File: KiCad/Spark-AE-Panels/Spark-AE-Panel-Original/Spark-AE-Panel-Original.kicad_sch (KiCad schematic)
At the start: 8 parts, among them U7 Connector_Micro_SD_Card_Yamai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

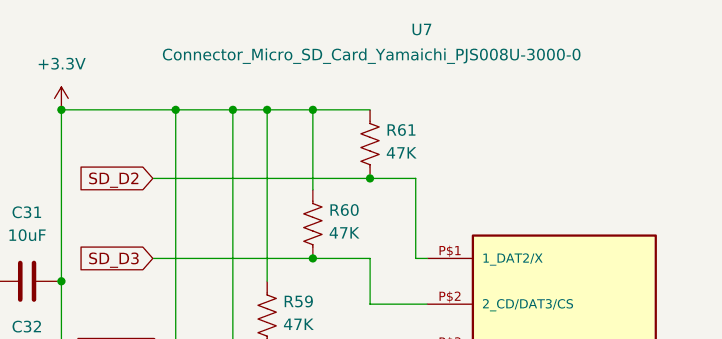
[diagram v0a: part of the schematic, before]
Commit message: rough pass over original mk0.1 panel. needs confirmation.
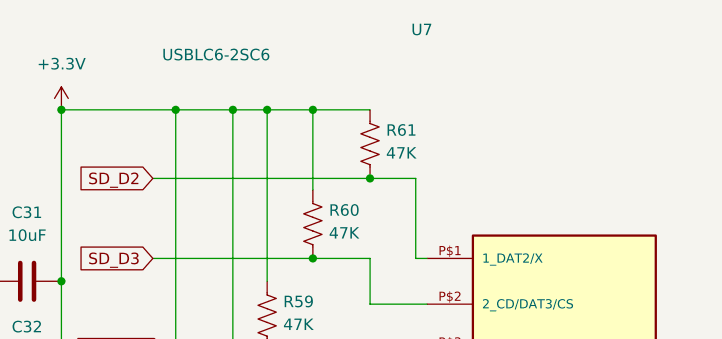
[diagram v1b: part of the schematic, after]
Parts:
- U7: value Connector_Micro_SD_Card_Yamaichi_PJS008U-3000-0 -> USBLC6-2SC6; footprint clectric-diy:PJS008U-3000-0 -> Package_TO_SOT_SMD:SOT-23-6; Availability In Stock -> (none); Check_prices https://www.snapeda.com/parts/PJS008U-3000-0/Yamaichi/view-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 -> (none); Description_1 8 Position Card Connector Secure Digital - microSD™ Through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 -> (none); MF Yamaichi -> (none); MP PJS008U-3000-0 -> (none); Package None -> (none); Price None -> (none); Purchase-URL https://www.snapeda.com/api/url_track_click_mouser/?unipart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 -> (none); SnapEDA_Link https://www.snapeda.com/parts/PJS008U-3000-0/Yamaichi/view-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 -> (none)
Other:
- title: Spark-AE -> Spark-AE-Panel-Original
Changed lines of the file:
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@@
 	(paper "A4")
 	(title_block
-		(title "Spark-AE")
-		(date "2026-01-14")
+		(title "Spark-AE-Panel-Original")
+		(date "2026-04-26")
+		(rev "Mk0.1")
 		(company "Copyright © 2026 clectric.diy Licensed under CERN-OHL-S v2")
 		(comment 1 "Charles H. Leggett")
@@
 		)
 		(instances
-			(project "Spark-AE-Panel"
+			(project "Spark-AE-Panel-Original"
 				(path "/3edf45fb-9cc6-4079-8dcc-c280276ec612"
 					(reference "R59")
@@
 		)
 		(instances
-			(project "Spark-AE-Panel"
+			(project "Spark-AE-Panel-Original"
 				(path "/3edf45fb-9cc6-4079-8dcc-c280276ec612"
 					(reference "#PWR066")
@@
 		)
 		(instances
-			(project "Spark-AE-Panel"
+			(project "Spark-AE-Panel-Original"
 				(path "/3edf45fb-9cc6-4079-8dcc-c280276ec612"
 					(reference "#PWR063")
@@
 			)
 		)
-		(property "Value" "Connector_Micro_SD_Card_Yamaichi_PJS008U-3000-0"
+		(property "Value" "USBLC6-2SC6"
 			(at 102.616 53.594 90)
 			(show_name no)
@@
 			)
 		)
-		(property "Footprint" "clectric-diy:PJS008U-3000-0"
+		(property "Footprint" "Package_TO_SOT_SMD:SOT-23-6"
 			(at 147.32 99.06 0)
 			(hide yes)
@@
 			)
 		)
-		(property "Datasheet" ""
+		(property "Datasheet" "https://www.st.com/resource/en/datasheet/usblc6-2.pdf"
 			(at 147.32 99.06 0)
 			(hide yes)
@@
 			)
 		)
-		(property "Description" ""
+		(property "Description" "Very low capacitance ESD protection diode, 2 data-line, SOT-23-6"
 			(at 147.32 99.06 0)
 			(hide yes)
@@
 			)
 		)
-		(property "MF" "Yamaichi"
-			(at 147.32 99.06 0)
-			(hide yes)
-			(show_name no)
-			(do_not_autoplace no)
-			(effects
-				(font
-					(size 1.27 1.27)
-				)
-				(justify bottom)
-			)
-		)
-		(property "Description_1" "8 Position Card Connector Secure Digital - microSD™ Through Hole Gold-Nickel"
-			(at 147.32 99.06 0)
-			(hide yes)
-			(show_name no)
-			(do_not_autoplace no)
-			(effects
-				(font
-					(size 1.27 1.27)
-				)
-				(justify bottom)
-			)
-		)
-		(property "Package" "None"
-			(at 147.32 99.06 0)
-			(hide yes)
-			(show_name no)
-			(do_not_autoplace no)
-			(effects
-				(font
-					(size 1.27 1.27)
-				)
-				(justify bottom)
-			)
-		)
-		(property "Price" "None"
-			(at 147.32 99.06 0)
-			(hide yes)
-			(show_name no)
-			(do_not_autoplace no)
-			(effects
-				(font
-					(size 1.27 1.27)
-				)
-				(justify bottom)
-			)
-		)
-		(property "SnapEDA_Link" "https://www.snapeda.com/parts/PJS008U-3000-0/Yamaichi/view-part/?ref=snap"
-			(at 147.32 99.06 0)
-			(hide yes)
-			(show_name no)
-			(do_not_autoplace no)
-			(effects
-				(font
-					(size 1.27 1.27)
-				)
-				(justify bottom)
-			)
-		)
-		(property "MP" "PJS008U-3000-0"
-			(at 147.32 99.06 0)
-			(hide yes)
-			(show_name no)
-			(do_not_autoplace no)
-			(effects
-				(font
-					(size 1.27 1.27)
-				)
-				(justify bottom)
-			)
-		)
-		(property "Purchase-URL" "https://www.snapeda.com/api/url_track_click_mouser/?unipart_id=493587&manufacturer=Yamaichi&part_name=PJS008U-3000-0&search_term=pjs008u-3000-0"
-			(at 147.32 99.06 0)
-			(hide yes)
-			(show_name no)
-			(do_not_autoplace no)
-			(effects
-				(font
-					(size 1.27 1.27)
-				)
-				(justify bottom)
-			)
-		)
-		(property "Availability" "In Stock"
-			(at 147.32 99.06 0)
-			(hide yes)
-			(show_name no)
-			(do_not_autoplace no)
-			(effects
-				(font
-					(size 1.27 1.27)
-				)
-				(justify bottom)
-			)
-		)
-		(property "Check_prices" "https://www.snapeda.com/parts/PJS008U-3000-0/Yamaichi/view-part/?ref=eda"
-			(at 147.32 99.06 0)
-			(hide yes)
-			(show_name no)
-			(do_not_autoplace no)
-			(effects
-				(font
-					(size 1.27 1.27)
-				)
-				(justify bottom)
-			)
-		)
 		(pin "P$9"
 		)
@@
 		)
 		(instances
-			(project "Spark-AE-Panel"
+			(project "Spark-AE-Panel-Original"
 				(path "/3edf45fb-9cc6-4079-8dcc-c280276ec612"
 					(reference "U7")
@@
 		)
 		(instances
-			(project "Spark-AE-Panel"
+			(project "Spark-AE-Panel-Original"
 				(path "/3edf45fb-9cc6-4079-8dcc-c280276ec612"
 					(reference "R61")
@@
 		)
 		(instances
-			(project "Spark-AE-Panel"
+			(project "Spark-AE-Panel-Original"
 				(path "/3edf45fb-9cc6-4079-8dcc-c280276ec612"
 					(reference "C31")
@@
 		)
 		(instances
-			(project "Spark-AE-Panel"
+			(project "Spark-AE-Panel-Original"
 				(path "/3edf45fb-9cc6-4079-8dcc-c280276ec612"
 					(reference "C32")
@@
 		)
 		(instances
-			(project "Spark-AE-Panel"
+			(project "Spark-AE-Panel-Original"
 				(path "/3edf45fb-9cc6-4079-8dcc-c280276ec612"
 					(reference "R58")
@@
 		)
 		(instances
-			(project "Spark-AE-Panel"
+			(project "Spark-AE-Panel-Original"
 				(path "/3edf45fb-9cc6-4079-8dcc-c280276ec612"
 					(reference "R60")
@@
 		)
 		(instances
-			(project "Spark-AE-Panel"
+			(project "Spark-AE-Panel-Original"
 				(path "/3edf45fb-9cc6-4079-8dcc-c280276ec612"
 					(reference "R57")
